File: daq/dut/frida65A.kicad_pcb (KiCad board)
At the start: 4 copper layers, 100 x 100 mm, 104 parts, among them J1 DisplayPort Molex 472720024, J10 VIN CFG, J11 TP AMP, J12 MiniFitJr Molex 469990014, J13 POWER, J14 RJ45 Molex 446200002, J15 SPI TP, J2 TP CLOCKS, J3 SMA Molex 733910070, J4 SMA Molex 733910070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

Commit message: Add support for image generation and outdir control
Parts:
- R27, R28, R29, R30: footprint Resistor_SMD:R_0402_1005Metric -> Resistor_SMD:R_0201_0603Metric; moved to B.Cu
- TH1: moved to B.Cu
- moved R28 87.8 mm to (121.7, 120.2), turned to 90 degrees
- moved R27 85.7 mm to (124.3, 120.2), turned to 90 degrees
- moved R30 84.4 mm to (129.4, 120.2), turned to 90 degrees
- moved R29 82.5 mm to (126.8, 120.2), turned to 90 degrees
- moved R34 46.0 mm to (173.0, 128.8), turned to -90 degrees
- moved U2 45.8 mm to (176.4, 126.5), turned to 90 degrees
- moved R36 45.5 mm to (166.5, 116.0)
- moved R35 43.6 mm to (172.1, 124.4), turned to 180 degrees
- moved R33 42.1 mm to (179.5, 128.8), turned to -90 degrees
- moved TH1 29.7 mm to (150.0, 100.7), turned to 180 degrees
- moved J15 20.0 mm to (168.4, 121.5), turned to 90 degrees
- moved C31 10.3 mm to (169.9, 131.5)
- moved C32 10.3 mm to (169.9, 130.4)
- moved C33 8.42 mm to (169.9, 127.4)
- moved C34 8.42 mm to (169.9, 126.3)
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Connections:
- J12 pad 1: Net-(FB1-Pad1) -> Net-(FB2-Pad1)
- J12 pad 2: Net-(FB3-Pad1) -> GND
- J12 pad 3: Net-(FB2-Pad1) -> Net-(FB3-Pad1)
- J12 pad 4: GND -> Net-(FB1-Pad1)
- J13 pad 2: /VDD_A -> /VDD_IO
- J13 pad 4: /VDD_IO -> /VDD_A
- J14 pad 1: /SPI_CS_B_EXT -> /SPI_SDO_EXT
- J14 pad 2: /SPI_SDO_EXT -> /SPI_CS_B_EXT
- J2 pad 5: /COMP_OUT_N -> /COMP_OUT_P
- J2 pad 6: /COMP_OUT_P -> /COMP_OUT_N
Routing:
- net Net-(J1-Pad14): track 9.43 -> 57.2 mm, vias 2 -> 1
- net Earth: track 0.00 -> 46.1 mm
- net Net-(J1-Pad13): track 11.5 -> 56.7 mm, vias 2 -> 1
- net /VDD_BDAQ: track 25.8 -> 53.6 mm, vias 1 -> 0
- net /VDD: track 19.1 -> 46.2 mm, vias 0 -> 1
- net /COMP_OUT_P: track 13.2 -> 35.6 mm
- net Net-(FB1-Pad1): track 23.4 -> 3.26 mm
- net GND: track 101.7 -> 120.1 mm, vias 44 -> 60
- net /VDD_IO: track 72.6 -> 89.6 mm
- net /COMP_OUT_N: track 19.3 -> 35.0 mm
- net /RST_B_EXT: track 21.8 -> 37.2 mm, vias 1 -> 0
- net /SPI_SDI_EXT: track 22.1 -> 36.1 mm, vias 1 -> 0
- net /SPI_SCLK_EXT: track 20.2 -> 32.9 mm
- net /VDD_D: track 61.6 -> 72.4 mm
- net Net-(FB3-Pad1): track 14.7 -> 4.16 mm
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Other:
- outline, holes or cut-outs redrawn

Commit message: Finish pcb layout
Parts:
- added REF**: FTD_Logo, frida:FTD_Logo, F.Cu at (120.7, 83.2)
- moved J10 76.4 mm to (154.0, 86.4), turned to -90 degrees
- moved R18 69.2 mm to (146.4, 69.8), turned to 90 degrees
- moved G*** 68.4 mm to (185.9, 87.6)
- moved J7 64.0 mm to (154.0, 72.7), turned to -90 degrees
- moved R15 61.6 mm to (154.0, 69.7), turned to 90 degrees
- moved J6 60.1 mm to (154.0, 64.0), turned to -90 degrees
- moved J9 59.1 mm to (169.3, 64.0), turned to -90 degrees
- moved R23 36.3 mm to (172.0, 67.0), turned to -90 degrees
- moved R24 23.9 mm to (159.1, 67.0), turned to 90 degrees
- moved C2 21.2 mm to (144.0, 80.2), turned to -90 degrees
- moved C3 20.5 mm to (145.1, 80.2), turned to -90 degrees
- moved C5 18.7 mm to (146.3, 80.2), turned to -90 degrees
- moved D2 16.3 mm to (142.3, 89.7)
- moved D1 15.3 mm to (158.2, 89.8), turned to 180 degrees
- moved R19 14.4 mm to (143.8, 63.5), turned to -90 degrees
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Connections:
- J6 pad 1: GND -> Net-(J6-Pin_1)
- J6 pad 2: Net-(J6-Pin_2) -> GND
- J6 pad 3: /VIN_P_EXT -> Net-(J6-Pin_1)
- J6 pad 4: Net-(J6-Pin_2) -> /VIN_P_EXT
- J6 pad 5: Net-(J5-Pin_2) -> Net-(J6-Pin_5)
- J6 pad 6: Net-(J6-Pin_6) -> Net-(J5-Pin_2)
- J6 pad 7: GND -> Net-(J6-Pin_5)
- J6 pad 8: Net-(J6-Pin_6) -> GND
- R19 pad 2: Net-(J6-Pin_6) -> Net-(J6-Pin_5)
- R20 pad 2: Net-(J6-Pin_2) -> Net-(J6-Pin_1)
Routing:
- net /VIN_N_EXT: track 0.85 -> 98.4 mm
- net /AMP_PD_EXT: track 0.00 -> 84.8 mm, vias 0 -> 4
- net /VIN_P_EXT: track 23.5 -> 97.6 mm, vias 1 -> 0
- net /VDD_DAC: track 55.6 -> 119.1 mm, vias 3 -> 4
- net /VOCM_EXT: track 3.14 -> 62.5 mm
- net /VDD_BDAQ: track 53.6 -> 112.2 mm, vias 0 -> 2
- net /VIN_P: track 10.8 -> 44.5 mm, vias 0 -> 1
- net /VIN_N: track 10.8 -> 37.6 mm, vias 0 -> 1
- net /AMP_PD_N: track 1.17 -> 22.2 mm, vias 1 -> 3
- net Net-(J5-Pin_2): track 0.00 -> 17.6 mm
- net (no net): track 12.3 -> 0.00 mm
- net Net-(J7-Pin_2): track 0.00 -> 10.5 mm
- net Net-(J7-Pin_6): track 0.00 -> 10.4 mm
- net /VS_N: track 59.5 -> 69.3 mm, vias 6 -> 7
- net GND: track 120.1 -> 113.0 mm, vias 60 -> 74
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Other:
- outline, holes or cut-outs redrawn
- board text added: "+"
- board text added: "-"
- board text added: "50Ω"
- board text added: "AMP_PD"
- board text added: "Attntr"
- board text added: "BDAQ-side SPI"
- board text added: "Buffer"
- board text added: "Bypass"
- board text added: "CLK_COMP_N"
- board text added: "CLK_COMP_P"
- board text added: "CLK_INIT_N"
- board text added: "CLK_INIT_P"
- board text added: "CLK_LOGIC_N"
- board text added: "CLK_LOGIC_P"
- board text added: "CLK_SAMP_N"
- board text added: "CLK_SAMP_P"
- board text added: "COMP_OUT_N"
- board text added: "COMP_OUT_P"
- board text added: "CS_B"
- board text added: "DUT-side"
- board text added: "DUT-side SPI"
- board text added: "Diff"
- board text added: "DiffAmp"
- board text added: "EXT-side"
- board text added: "FRIDA 65a SCC v1"
- board text added: "GND"
- board text added: "Open"
- board text added: "RST_B"
- board text added: "SCLK"
- board text added: "SDI"
- board text added: "SDO"
- board text added: "SE"
- board text added: "VDD"
- board text added: "VDD_A"
- board text added: "VDD_BDAQ"
- board text added: "VDD_D"
- board text added: "VDD_DAC"
- board text added: "VDD_IO"
- board text added: "VIN_N"
- board text added: "VIN_P"
- board text added: "VOCM"
- board text added: "VS_N"
- board text added: "VS_P"

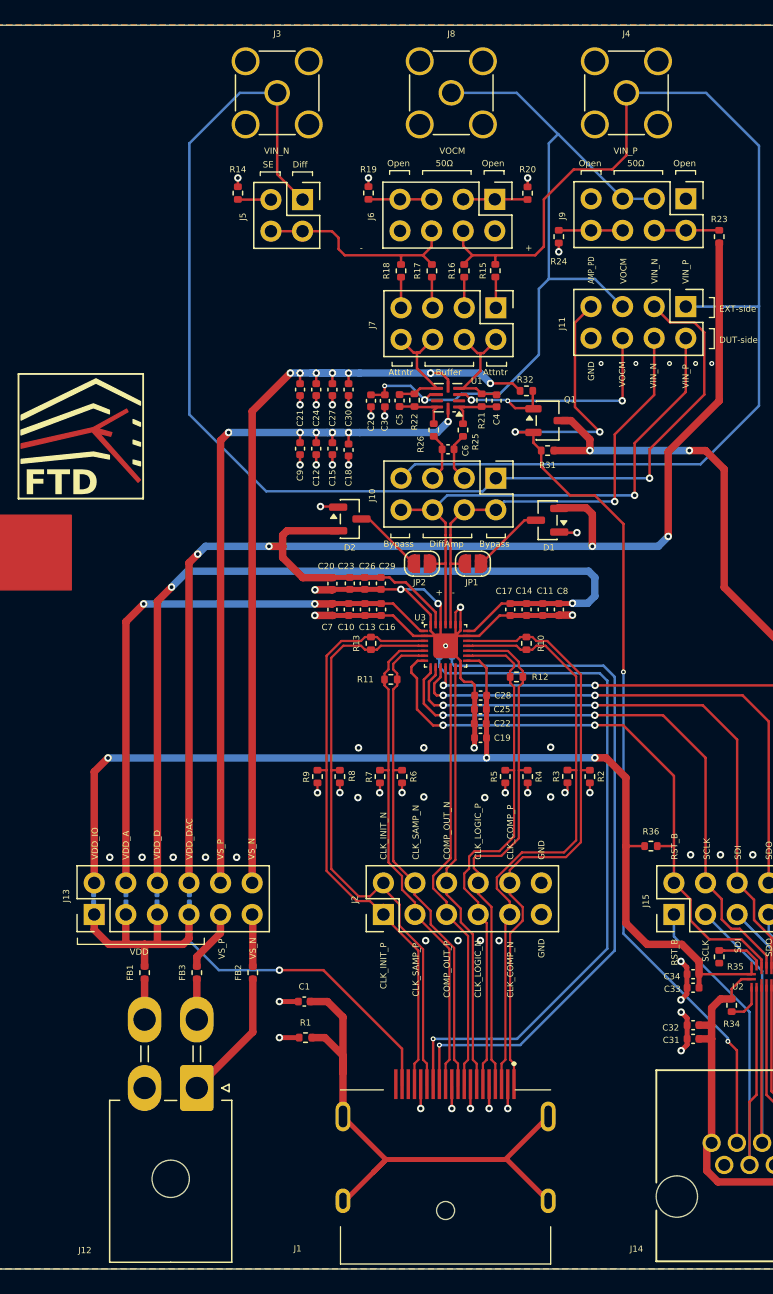
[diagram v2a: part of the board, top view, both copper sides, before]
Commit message: Update pcb layout post drc cleanup
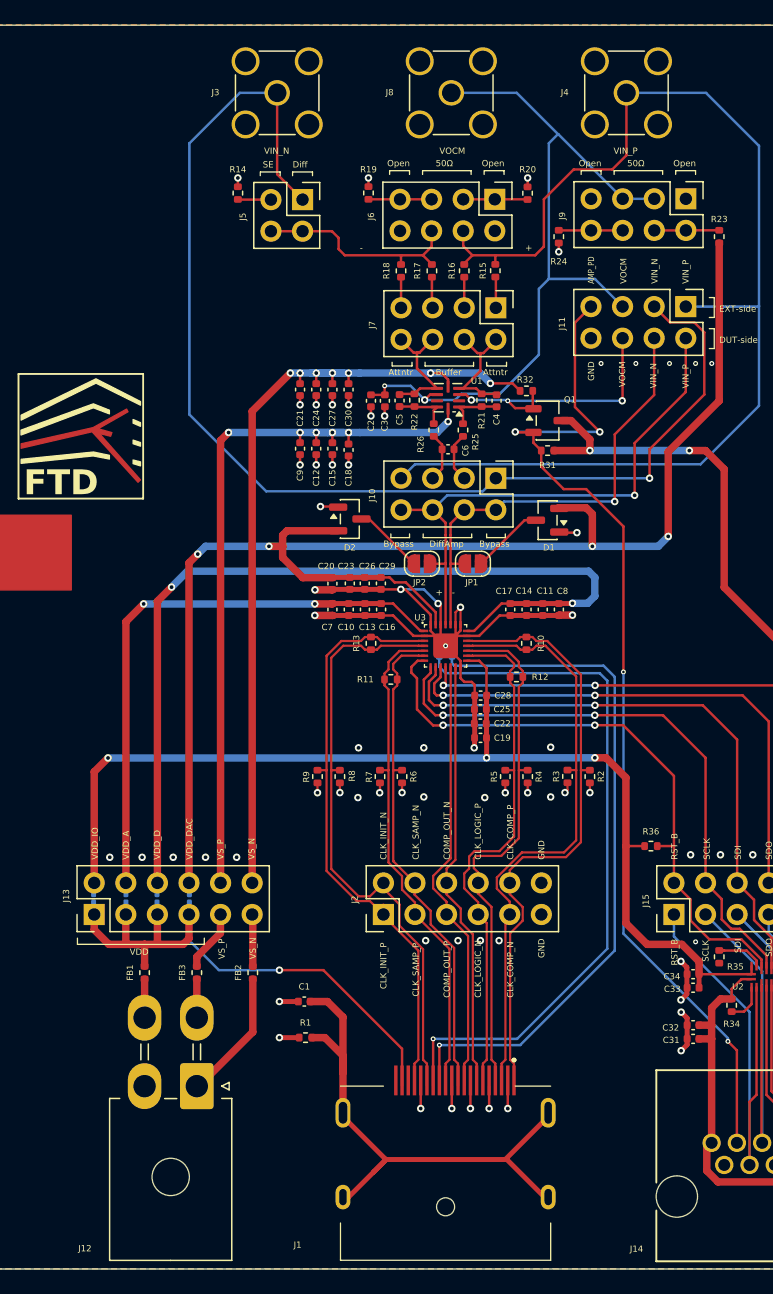
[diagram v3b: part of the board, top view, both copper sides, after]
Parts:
- moved J1 0.30 mm to (150.0, 141.2)
- moved J12 0.15 mm to (130.0, 135.3)
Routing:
- net GND: vias 74 -> 75
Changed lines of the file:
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@@
 		(tags "Molex SMA THT Female Jack Vertical 733910070")
 		(property "Reference" "J8"
-			(at 0 -4.75 0)
+			(at -4.96 -0.04 0)
 			(unlocked yes)
 			(layer "F.SilkS")
@@
 		(tags "Molex SMA THT Female Jack Vertical 733910070")
 		(property "Reference" "J4"
-			(at 0 -4.75 0)
+			(at -4.96 -0.04 0)
 			(unlocked yes)
 			(layer "F.SilkS")
@@
 	(footprint "frida:Molex_MiniFitJr_469990014"
 		(layer "F.Cu")
-		(at 130 135.45 180)
+		(at 130 135.3 180)
 		(descr "Molex Mini-Fit Jr. Power Connector, Part Number: 469990014, Series: 5569-04A2, 2x2 (4 circuits), Snap-in Plastic Peg PCB Lock, horizontal")
 		(tags "connector Molex Mini-Fit_Jr horizontalplastic_peg")
@@
 	(footprint "frida:Molex_DisplayPort_472720024"
 		(layer "F.Cu")
-		(at 150 141.5)
+		(at 150 141.2)
 		(descr "Molex DisplayPort Receptacle, Part Number: 472720024, 20-pin, right-angle, SMD")
 		(tags "Connector")
@@
 		(tags "Molex SMA THT Female Jack Vertical 733910070")
 		(property "Reference" "J3"
-			(at 0 -4.75 0)
+			(at -4.96 -0.04 0)
 			(unlocked yes)
 			(layer "F.SilkS")
@@
 	)
 	(via
+		(at 170.1 123.7)
+		(size 0.4)
+		(drill 0.2)
+		(layers "F.Cu" "B.Cu")
+		(free yes)
+		(net 1)
+	)
+	(via
 		(at 158.45 108.05)
 		(size 0.6)
@@
 	)
 	(segment
+		(start 136.9 91.9)
+		(end 135.8 91.9)
+		(width 0.6)
+		(layer "F.Cu")
+		(net 4)
+	)
+	(segment
 		(start 140.92 94.4)
 		(end 140.9 94.42)
@@
 	)
 	(segment
-		(start 136.9 91.9)
-		(end 135.8 91.9)
-		(width 0.6)
-		(layer "F.Cu")
-		(net 4)
-	)
-	(segment
 		(start 130.075 92.525)
 		(end 129.37 93.23)
@@
 	)
 	(segment
-		(start 155.64 82.74)
-		(end 155.6 82.7)
+		(start 164.3 102)
+		(end 164.3 90.3)
 		(width 0.2)
 		(layer "F.Cu")
@@
 	)
 	(segment
-		(start 160.4 73.915)
-		(end 161.69 72.625)
+		(start 155.64 82.74)
+		(end 155.6 82.7)
 		(width 0.2)
 		(layer "F.Cu")
@@
 	)
 	(segment
-		(start 164.3 102)
-		(end 164.3 90.1)
+		(start 160.4 73.915)
+		(end 161.69 72.625)
 		(width 0.2)
 		(layer "F.Cu")
@@
 	)
 	(segment
-		(start 173.42 132.42)
-		(end 172.7 131.7)
+		(start 164.3 90.3)
+		(end 161.3 87.3)
 		(width 0.2)
 		(layer "F.Cu")
@@
 	)
 	(segment
-		(start 157.0625 82.74)
-		(end 155.64 82.74)
+		(start 157.69 85.49)
+		(end 157.69 84.2)
 		(width 0.2)
 		(layer "F.Cu")
@@
 	)
 	(segment
-		(start 162 87.8)
-		(end 160 87.8)
+		(start 161.3 87.3)
+		(end 159.5 87.3)
 		(width 0.2)
 		(layer "F.Cu")
@@
 	)
 	(segment
-		(start 157.0625 83.5725)
-		(end 157.69 84.2)
+		(start 173.42 132.42)
+		(end 172.7 131.7)
 		(width 0.2)
 		(layer "F.Cu")
@@
 	)
 	(segment
-		(start 160 87.8)
-		(end 157.69 85.49)
+		(start 157.0625 82.74)
+		(end 155.64 82.74)
 		(width 0.2)
 		(layer "F.Cu")
@@
 	)
 	(segment
-		(start 173.42 139.8585)
-		(end 173.42 132.42)
+		(start 159.5 87.3)
+		(end 157.69 85.49)
 		(width 0.2)
 		(layer "F.Cu")
@@
 	)
 	(segment
-		(start 162.4 82.7)
-		(end 160.4 80.7)
+		(start 157.0625 83.5725)
+		(end 157.69 84.2)
 		(width 0.2)
 		(layer "F.Cu")
@@
 	)
 	(segment
-		(start 164.3 90.1)
-		(end 162 87.8)
+		(start 173.42 139.8585)
+		(end 173.42 132.42)
 		(width 0.2)
 		(layer "F.Cu")
@@
 	)
 	(segment
-		(start 157.69 85.49)
-		(end 157.69 84.2)
+		(start 162.4 82.7)
+		(end 160.4 80.7)
 		(width 0.2)
 		(layer "F.Cu")

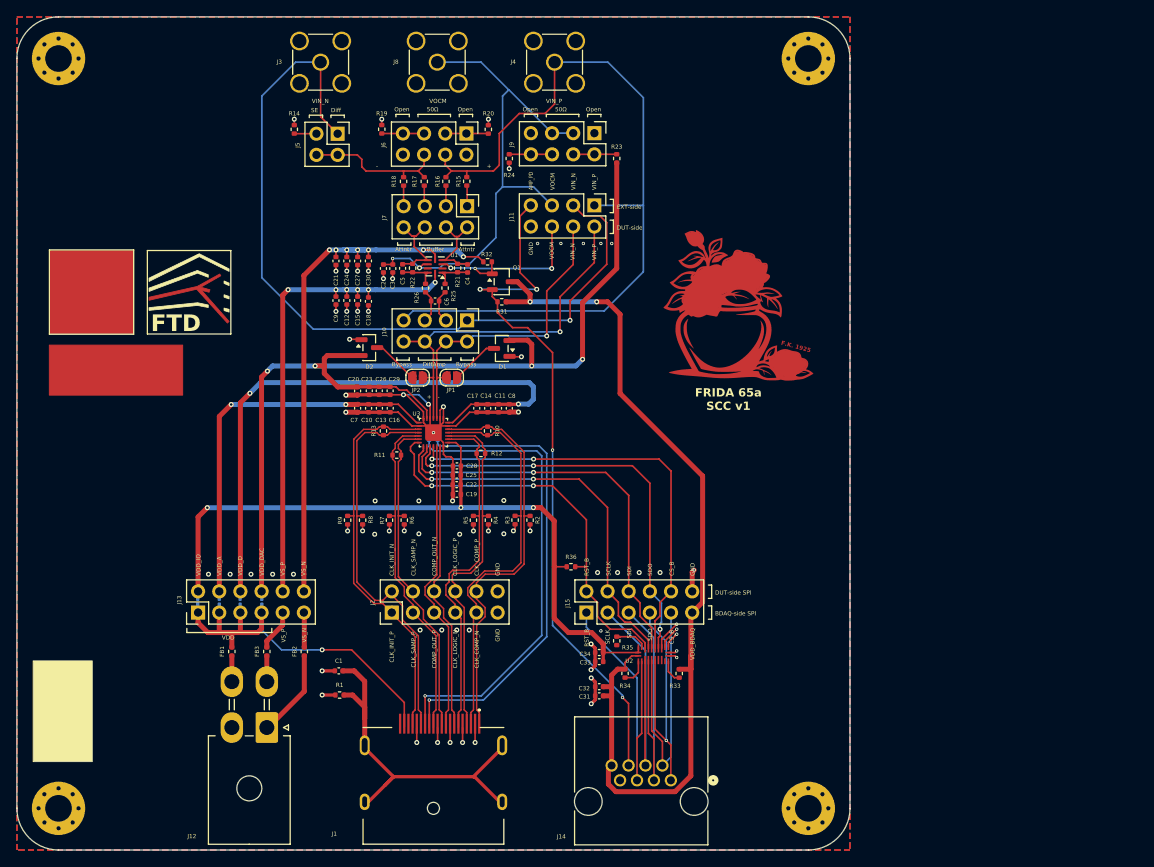
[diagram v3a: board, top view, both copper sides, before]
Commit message: feat(aor): expand comparator place-and-route flow, add DEF-to-GDS scripts, update placement
Add def2gds.py, gen_macros_gds.py for GDS export from OpenROAD DEF,
add sg13g2.lyt/.map KLayout tech files, replace notes.md with plan.md,
enlarge floorplan to 35x35 um with 8-row symmetric placement,
fix LEF pin sizes for track alignment, remove Metal1 OBS,
add layout subcommand to CLI, add ODB reference docs.
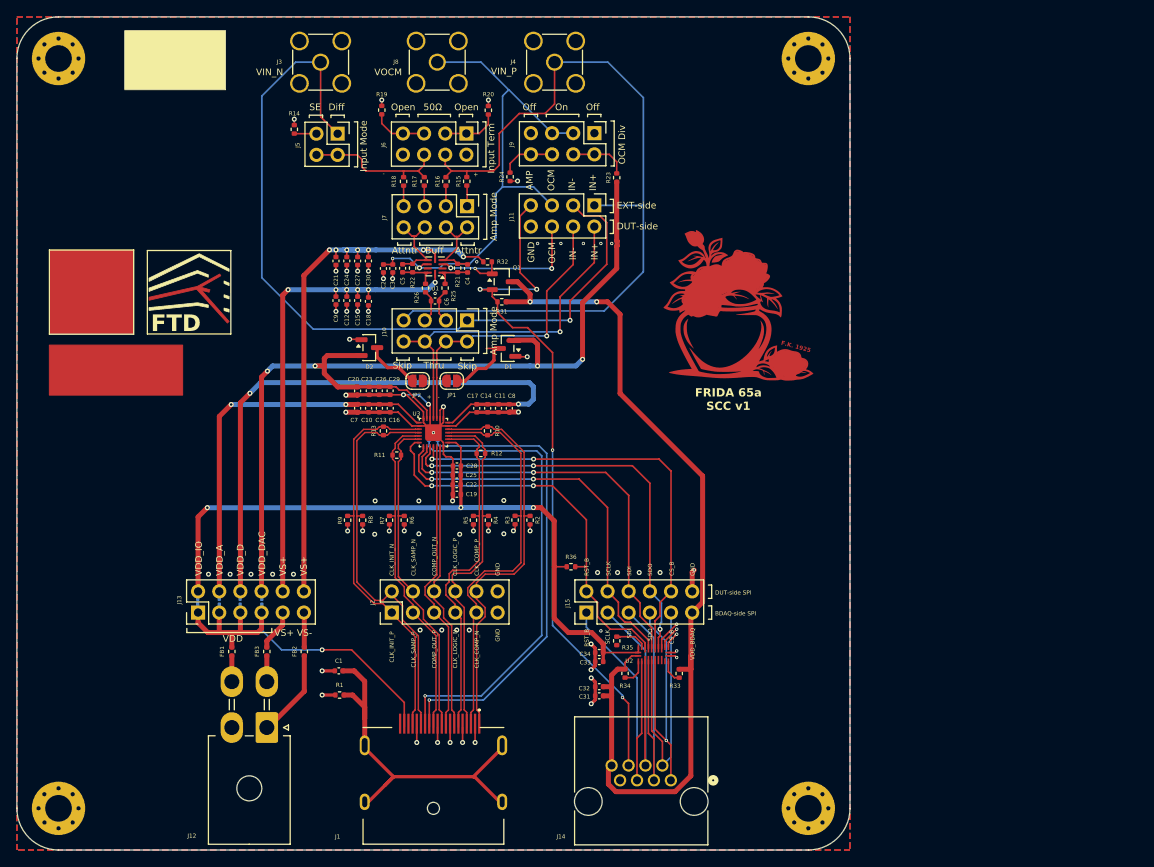
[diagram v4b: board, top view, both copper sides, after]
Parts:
- moved R19 2.30 mm to (143.8, 61.2)
- moved R20 2.30 mm to (156.6, 61.2)
- moved R23 2.30 mm to (172.0, 69.3)
- moved R24 2.20 mm to (159.2, 69.2)
- moved D1 0.70 mm to (158.9, 89.8)
- moved JP1 0.40 mm to (152.2, 93.7)
- moved JP2 0.40 mm to (148.1, 93.7)
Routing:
- net /VDD_DAC: track 119.1 -> 116.8 mm
- net Net-(JP1-A): track 5.76 -> 7.68 mm
- net Net-(J9-Pin_2): track 5.22 -> 7.08 mm
- net Net-(J6-Pin_1): track 5.18 -> 6.84 mm
- net Net-(J6-Pin_5): track 5.08 -> 6.67 mm
- net Net-(JP2-B): track 5.70 -> 7.15 mm
- net Net-(J9-Pin_6): track 5.14 -> 6.59 mm
- net /VIN_P: track 44.5 -> 43.2 mm
- net /VIN_N: track 37.6 -> 36.5 mm
- net GND: track 113.0 -> 113.2 mm, vias 75 -> 77
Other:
- board text added: "AMP"
- board text added: "Amp Mode"
- board text added: "Buff"
- board text added: "IN+"
- board text added: "IN-"
- board text added: "Input Mode"
- board text added: "Input Term"
- board text added: "OCM"
- board text added: "OCM Div"
- board text added: "Off"
- board text added: "On"
- board text added: "Skip"
- board text added: "Thru"
- board text added: "VS+"
- board text added: "VS-"
- board text removed: "AMP_PD"
- board text removed: "Buffer"
- board text removed: "Bypass"
- board text removed: "DiffAmp"
- board text removed: "VS_N"
- board text removed: "VS_P"
